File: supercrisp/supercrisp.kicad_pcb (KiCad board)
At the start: 2 copper layers, 140 x 91 mm, 135 parts, among them J1 SWD, J2 SWD, P1 USB_C_Plug_USB2.0, P2 USB_C_Plug_USB2.0, SW1 SW_Push, SW10 SW_Push, SW11 SW_Push, SW12 SW_Push, SW13 SW_Push, SW14 SW_Push, SW15 SW_Push, SW16 SW_Push, SW17 SW_Push, SW18 SW_Push, SW19 SW_Push, SW2 SW_Push, SW20 SW_Push, SW21 SW_Push, SW22 SW_Push, SW23 SW_Push, SW24 SW_Push, SW25 SW_Push, SW26 SW_Push, SW27 SW_SPDT, SW28 SW_SPDT, SW3 SW_Push, SW4 SW_Push, SW5 SW_Push, SW6 SW_Push, SW7 SW_Push, SW8 SW_Push, SW9 SW_Push, U1 USBLC6-2SC6, U2 TPS82140, U3 USBLC6-2SC6, U6 TPS82140

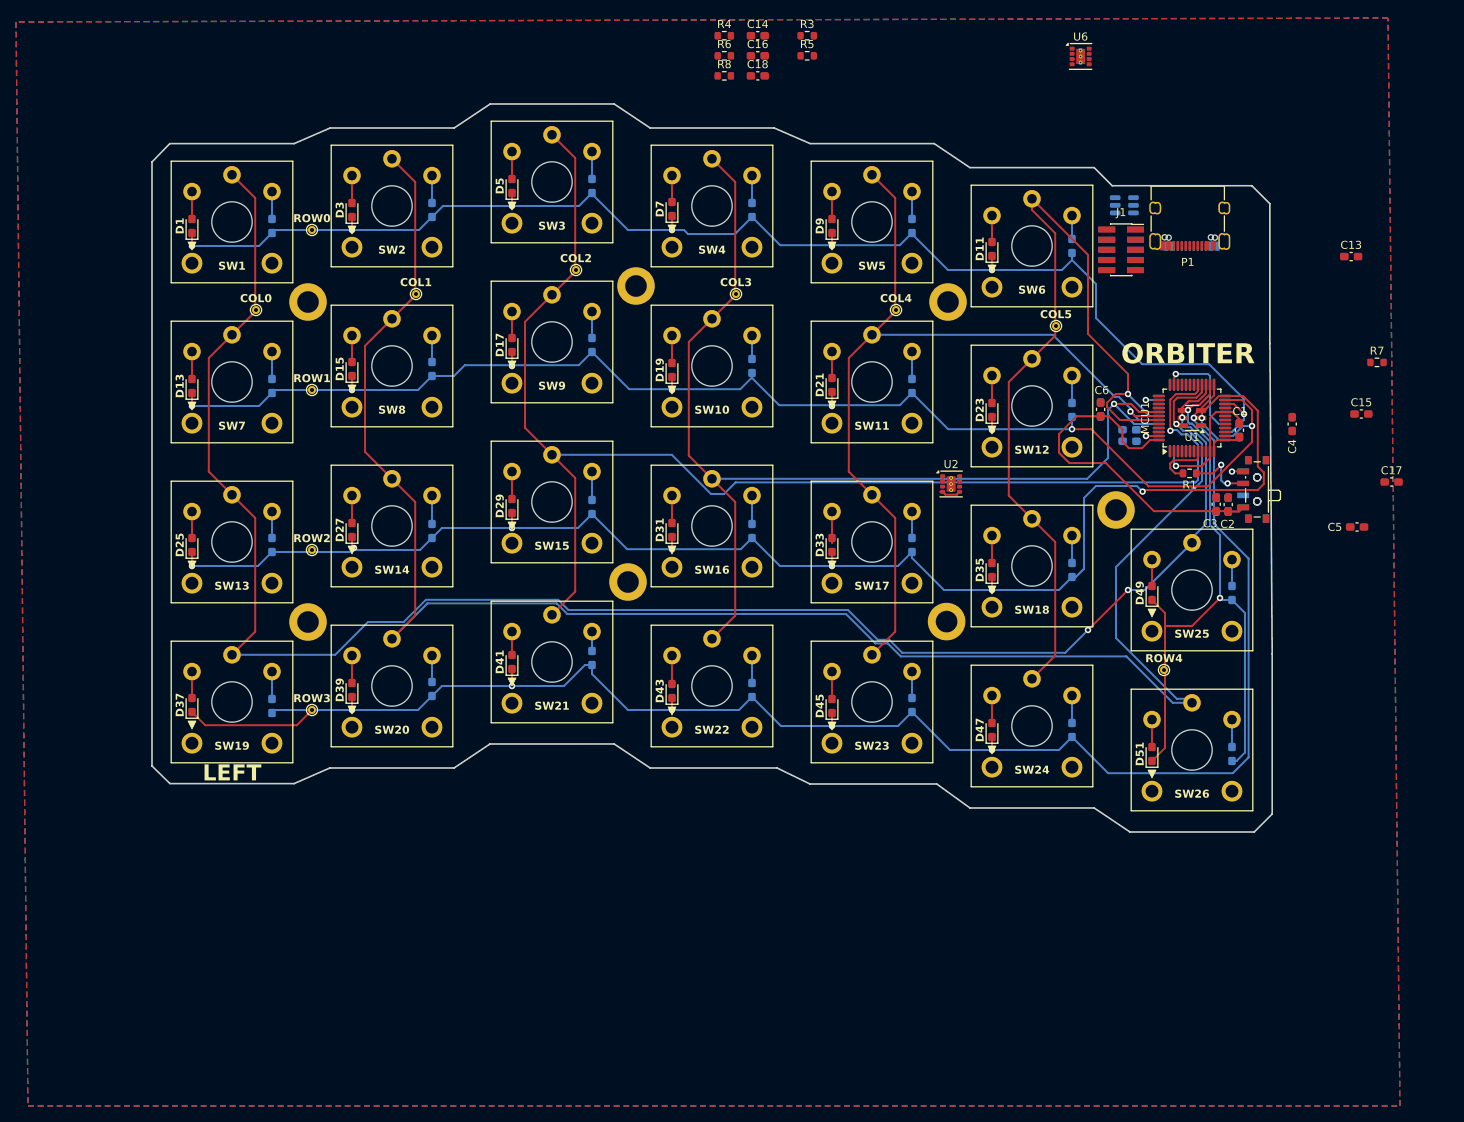
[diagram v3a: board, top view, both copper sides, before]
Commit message: Continue placing components for USB
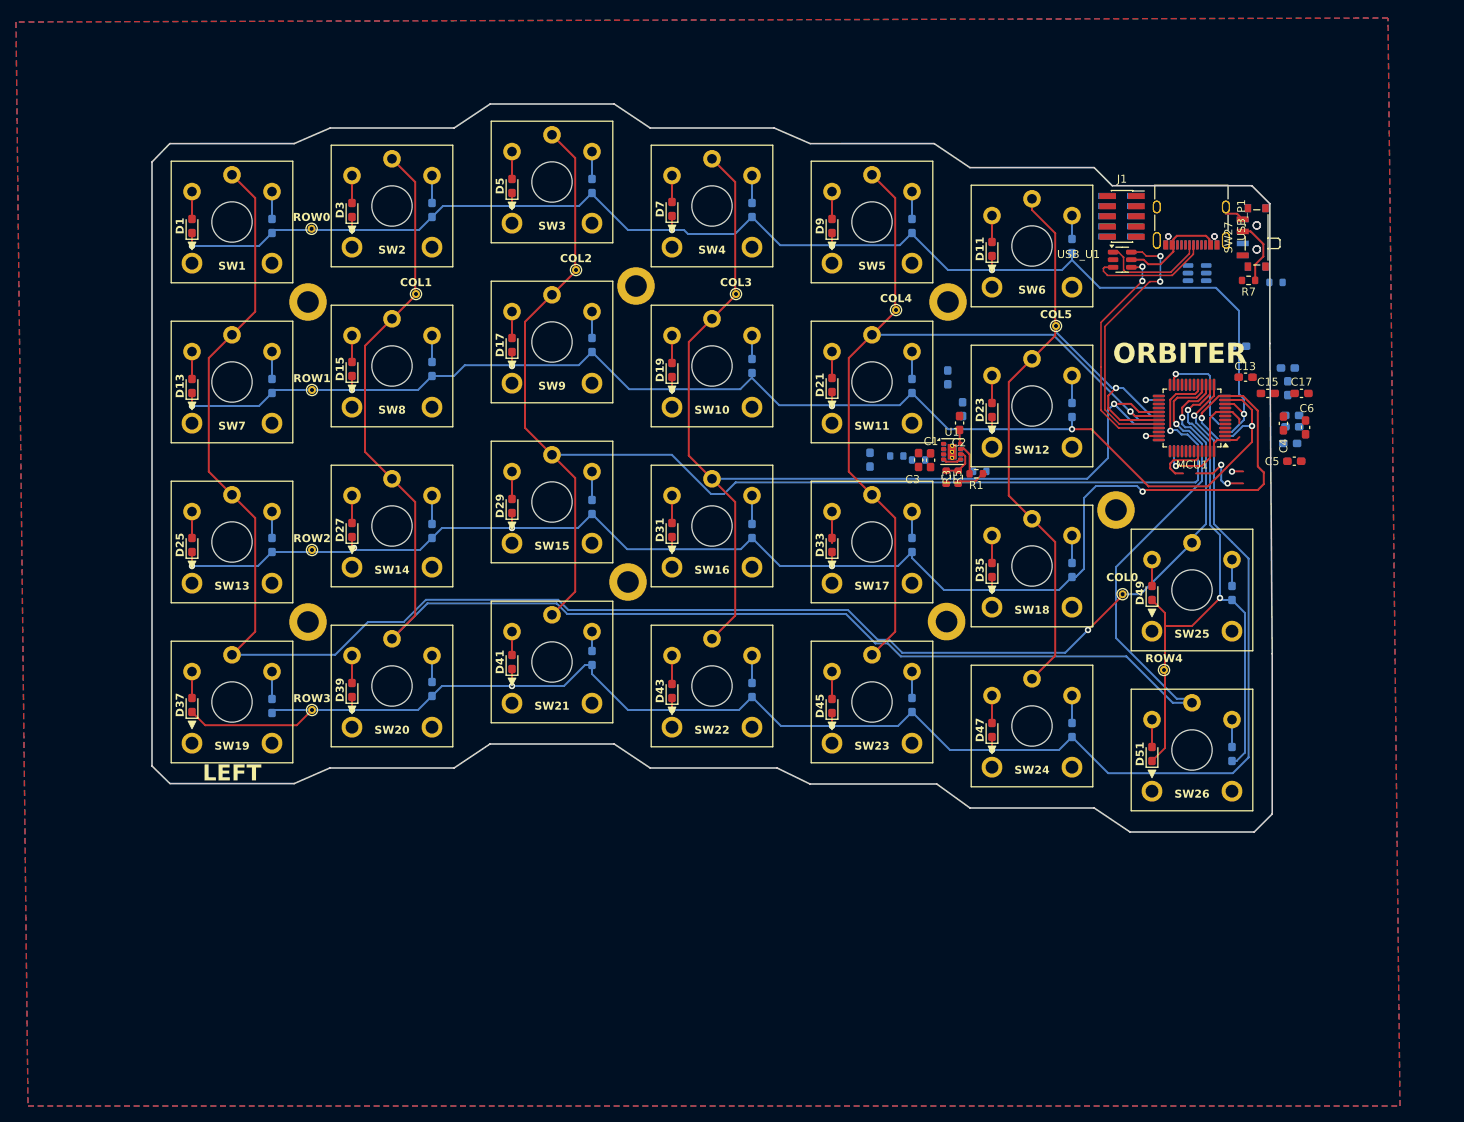
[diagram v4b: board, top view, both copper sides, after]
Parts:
- removed P1, P2: USB_C_Plug_USB2.0, Connector_USB:USB_C_Receptacle_XKB_U262-16XN-4BVC11
- removed U2, U6: TPS82140, Package_LGA:Texas_SIL0008D_MicroSiP-8-1EP_2.8x3mm_P0.65mm_EP1.1x1.9mm_ThermalVias
- removed U3: USBLC6-2SC6, Package_TO_SOT_SMD:SOT-23-6
- added U4: TPS82140, Package_LGA:Texas_SIL0008D_MicroSiP-8-1EP_2.8x3mm_P0.65mm_EP1.1x1.9mm_ThermalVias, B.Cu at (170.0, 73.8)
- added USB_P1: USB_C_Plug_USB2.0, Connector_USB:USB_C_Receptacle_XKB_U262-16XN-4BVC11, F.Cu at (199.9, 44.2)
- added USB_P2: USB_C_Plug_USB2.0, Connector_USB:USB_C_Receptacle_XKB_U262-16XN-4BVC11, B.Cu at (199.9, 44.2)
- added USB_U1: USBLC6-2SC6, Package_TO_SOT_SMD:SOT-23-6, F.Cu at (191.3, 49.7)
- added USB_U2: USBLC6-2SC6, Package_TO_SOT_SMD:SOT-23-6, B.Cu at (200.6, 51.4)
- C10: value 100n -> 4u7
- C14: value 430pF -> 100n; moved to B.Cu
- C16, C18: value 22uF -> 100n; moved to B.Cu
- C7: value 4u7 -> 22uF
- C8: value 100n -> 430pF
- C9: value 100n -> 22uF
- R2: value 10k -> 100k
- R4: value 100k -> 309k; moved to B.Cu
- R6: value 309k -> 100k; moved to B.Cu
- R8: value 100k -> 10k; moved to B.Cu
- SW4: moved to B.Cu
- U1: value USBLC6-2SC6 -> TPS82140; footprint Package_TO_SOT_SMD:SOT-23-6 -> Package_LGA:Texas_SIL0008D_MicroSiP-8-1EP_2.8x3mm_P0.65mm_EP1.1x1.9mm_ThermalVias
- moved COL0 114.0 mm to (191.3, 91.5)
- moved C14 83.8 mm to (212.3, 72.7), turned to 180 degrees
- moved C16 76.9 mm to (212.0, 63.2), turned to 180 degrees
- moved R8 73.6 mm to (210.5, 52.5), turned to 180 degrees
- moved C18 69.0 mm to (205.9, 60.5)
- moved R6 61.0 mm to (173.5, 76.2), turned to 180 degrees
- moved R3 58.3 mm to (170.8, 76.9), turned to 90 degrees
- moved R4 56.8 mm to (163.1, 74.2), turned to 180 degrees
- moved R5 55.5 mm to (169.3, 76.9), turned to -90 degrees
- moved C9 43.6 mm to (159.8, 74.7)
- moved C1 38.8 mm to (167.3, 74.8)
- moved C3 37.6 mm to (165.8, 74.8)
- moved C7 37.0 mm to (169.5, 64.4)
- moved C8 35.3 mm to (171.3, 68.4)
- moved C2 35.1 mm to (170.9, 70.1)
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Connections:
- C14 pad 1: Net-(U6-SS/TR) -> /MCU_BOTTOM/VOUT_3V3
- C16 pad 1: /MCU_BOTTOM/VBUS -> /MCU_BOTTOM/VOUT_3V3
- C2 pad 1: Net-(U2-SS/TR) -> Net-(U1-SS/TR)
- C7 pad 1: /MCU_BOTTOM/VOUT_3V3 -> /MCU_BOTTOM/VBUS
- C8 pad 1: /MCU_BOTTOM/VOUT_3V3 -> Net-(U4-SS/TR)
- R1 pad 2: Net-(U2-PG) -> Net-(U1-PG)
- R2 pad 1: Net-(SW28-B) -> /MCU_BOTTOM/VOUT_3V3
- R2 pad 2: /MCU_BOTTOM/BOOT0 -> Net-(U4-PG)
- R3 pad 2: Net-(U2-FB) -> Net-(U1-FB)
- R4 pad 1: Net-(U6-FB) -> /MCU_BOTTOM/VOUT_3V3
- R4 pad 2: GND -> Net-(U4-FB)
- R5 pad 1: Net-(U2-FB) -> Net-(U1-FB)
- R6 pad 1: /MCU_BOTTOM/VOUT_3V3 -> Net-(U4-FB)
- R6 pad 2: Net-(U6-FB) -> GND
- R8 pad 1: /MCU_BOTTOM/VOUT_3V3 -> Net-(SW28-B)
- R8 pad 2: Net-(U6-PG) -> /MCU_BOTTOM/BOOT0
- U1 pad 1: /MCU_TOP/USB_CONN_D- -> /MCU_TOP/VBUS
- U1 pad 2: GND -> /MCU_TOP/VBUS
- U1 pad 3: /MCU_TOP/USB_CONN_D+ -> GND
- U1 pad 4: /MCU_TOP/USB_D+ -> /MCU_TOP/VOUT_3V3
- U1 pad 5: /MCU_TOP/VBUS -> /MCU_TOP/VOUT_3V3
- U1 pad 6: /MCU_TOP/USB_D- -> Net-(U1-FB)
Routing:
- net (no net): track 49.4 -> 0.00 mm
- net /MCU_TOP/USB_D-: track 0.00 -> 34.3 mm, vias 0 -> 2
- net /MCU_TOP/USB_D+: track 0.00 -> 29.7 mm, vias 0 -> 2
- net /T_MCU_COL5: track 112.3 -> 95.0 mm
- net /MCU_TOP/USB_CONN_D+: track 0.00 -> 15.9 mm
- net /MCU_TOP/USB_CONN_D-: track 0.00 -> 13.6 mm
- net /MCU_TOP/VBUS: track 0.65 -> 13.5 mm
- net Net-(SW27-B): track 8.68 -> 16.9 mm
- net /MCU_TOP/VOUT_3V3: track 2.73 -> 10.9 mm
- net Net-(U1-FB): track 0.00 -> 4.43 mm
- net Net-(U1-PG): track 0.00 -> 3.76 mm
- net /T_MCU_ROW0: track 170.9 -> 174.5 mm
- net GND: track 34.6 -> 37.0 mm
- net Net-(U1-SS/TR): track 0.00 -> 1.69 mm
- net /T_MCU_COL0: track 222.5 -> 222.7 mm, vias 3 -> 2
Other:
- board text removed: "GTB 0x01"
